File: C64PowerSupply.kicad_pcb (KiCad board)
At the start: 2 copper layers, 127 x 61 mm, 17 parts, among them J1 120V IN, J2 OUT, U1 LM2596T-ADJ

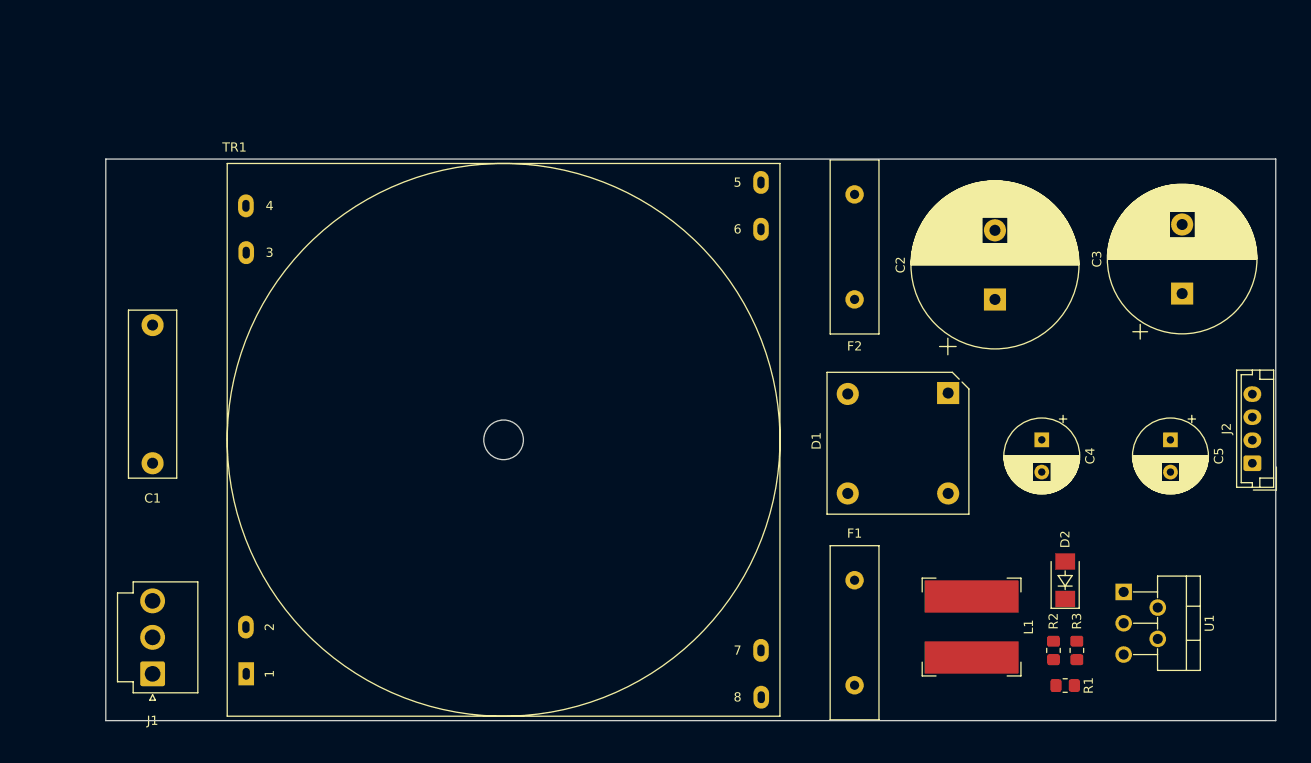
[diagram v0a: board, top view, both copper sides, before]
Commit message: Footprints, layout
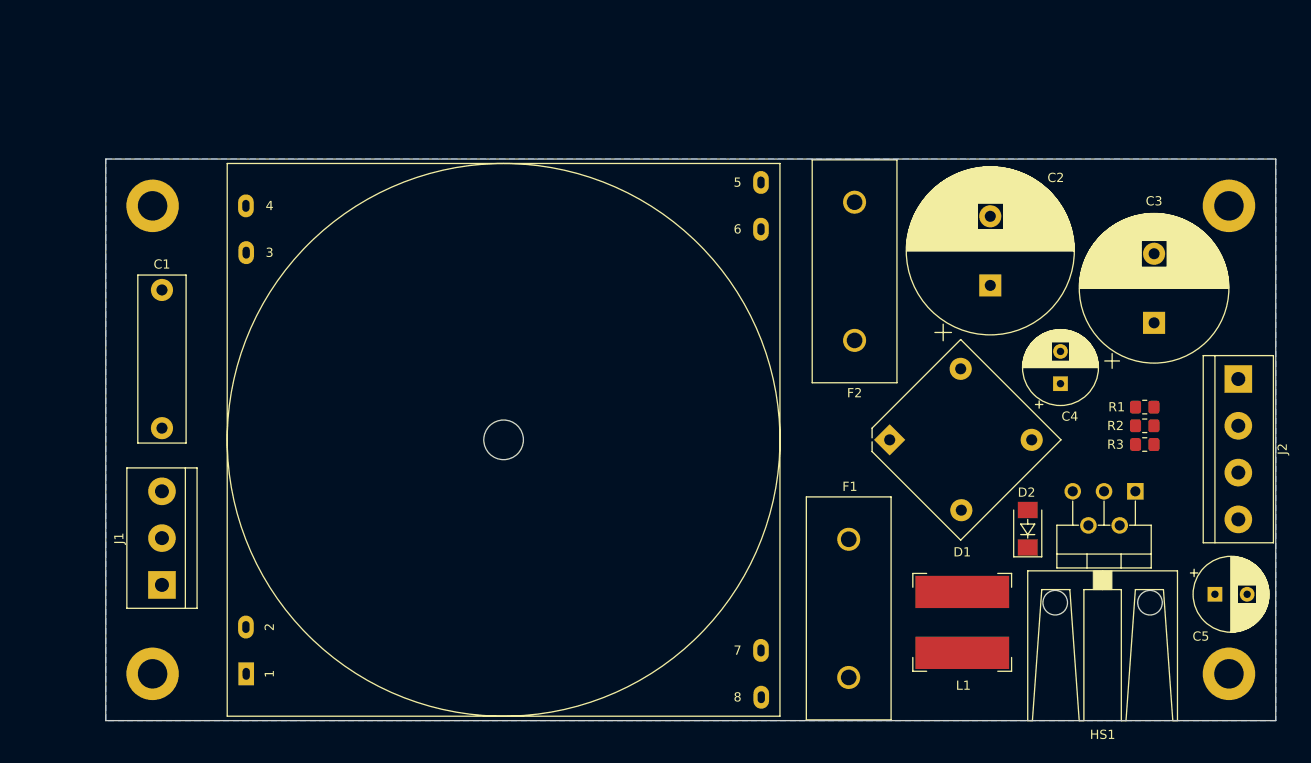
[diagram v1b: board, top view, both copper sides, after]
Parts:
- added H1: M3, MountingHole:MountingHole_3.2mm_M3_ISO7380_Pad, F.Cu at (73.7, 71.1)
- added H2: M3, MountingHole:MountingHole_3.2mm_M3_ISO7380_Pad, F.Cu at (190.5, 71.1)
- added H3: M3, MountingHole:MountingHole_3.2mm_M3_ISO7380_Pad, F.Cu at (190.5, 121.9)
- added H4: M3, MountingHole:MountingHole_3.2mm_M3_ISO7380_Pad, F.Cu at (73.7, 121.9)
- added HS1: Heatsink, DTLib:AAVID581002B02500G, F.Cu at (176.8, 110.7)
- F1, F2: footprint Fuse:Fuse_Littelfuse-LVR100 -> DTLib:Fuse_PTF-76
- J1: footprint Connector_JST:JST_VH_B3P-VH-B_1x03_P3.96mm_Vertical -> TerminalBlock:TerminalBlock_bornier-3_P5.08mm
- J2: footprint Connector_JST:JST_EH_B4B-EH-A_1x04_P2.50mm_Vertical -> TerminalBlock:TerminalBlock_bornier-4_P5.08mm
- moved R1 31.4 mm to (181.4, 93.0)
- moved R2 26.3 mm to (181.4, 95.0), turned to 180 degrees
- moved R3 23.5 mm to (181.4, 97.0), turned to 0 degrees
- moved C5 17.4 mm to (189.0, 113.3), turned to 0 degrees
- moved U1 11.0 mm to (180.3, 102.1), turned to 180 degrees
- moved J1 9.71 mm to (74.7, 112.3)
- moved J2 9.27 mm to (191.5, 89.9), turned to 270 degrees
- moved D1 8.13 mm to (153.7, 96.5), turned to 45 degrees
- moved D2 6.91 mm to (168.7, 106.2)
- moved C4 6.43 mm to (172.2, 90.4), turned to 90 degrees
- moved F1 4.49 mm to (149.2, 107.3)
- moved F2 4.44 mm to (149.9, 85.7)
- moved C3 4.40 mm to (182.4, 83.8)
- moved C1 3.94 mm to (74.7, 95.2)
- moved C2 1.61 mm to (164.6, 79.8)
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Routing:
- added copper zone on B.Cu, net GND

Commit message: Routing
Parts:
- R1, R2, R3: moved to B.Cu
- moved R1 20.3 mm to (176.8, 112.8)
- moved R2 16.4 mm to (176.8, 110.7), turned to 0 degrees
- moved F1 15.1 mm to (149.2, 122.4), turned to 90 degrees
- moved R3 12.5 mm to (176.8, 108.7), turned to 180 degrees
- moved C4 9.33 mm to (180.3, 95.0), turned to 180 degrees
- moved C5 1.02 mm to (188.0, 113.3)
- moved F2 0.51 mm to (149.4, 85.7)
- moved J2 0.51 mm to (191.0, 89.9)
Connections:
- net Net-(F1-Pad1) renamed /9VAC+
- net Net-(J2-Pad3) renamed /9VAC-
- J1 pad 1: /HOT -> GND
- J1 pad 3: GND -> /HOT
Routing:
- net GND: track 0.00 -> 308.1 mm
- net /9VAC-: track 0.00 -> 83.7 mm
- net /9VAC+: track 0.00 -> 67.8 mm
- net /VUNREG: track 0.00 -> 62.2 mm
- net VCC: track 0.00 -> 61.4 mm
- net /NEUTRAL: track 0.00 -> 57.0 mm
- net /HOT: track 0.00 -> 55.8 mm
- net Net-(D1-Pad2): track 0.00 -> 48.9 mm
- net Net-(F1-Pad2): track 0.00 -> 26.7 mm
- net /REG-OUT: track 0.00 -> 20.1 mm
- net Net-(D1-Pad4): track 0.00 -> 13.3 mm
- net Net-(F2-Pad2): track 0.00 -> 10.9 mm
- net /VADJ: track 0.00 -> 6.19 mm
- net Net-(R1-Pad2): track 0.00 -> 2.03 mm
- added copper zone on F.Cu, net GND
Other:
- net class MAINS added: clearance 0.5, trace_width 1, via_dia 1, via_drill 0.6
- board text added: "5VDC"
- board text added: "9VAC"
- board text added: "C64 Power Supply RevA 2021 Dominic Thibodeau https://github.com/hotkeysoft/c64PowerSupply-kicad dev@hotkeysoft.net"
- board text added: "GND"
- board text added: "H"
- board text added: "JLCJLCJLCJLC"
- board text added: "N"
- board text added: "WARNING 120 VAC"

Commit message: Added trimpot. Routing
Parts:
- removed R1: 4.7K, Resistor_SMD:R_0805_2012Metric_Pad1.20x1.40mm_HandSolder
- added RV1: 2K, Potentiometer_THT:Potentiometer_Bourns_3266W_Vertical, F.Cu at (179.3, 90.4)
- J1: footprint TerminalBlock:TerminalBlock_bornier-3_P5.08mm -> TerminalBlock_Phoenix:TerminalBlock_Phoenix_PT-1,5-3-5.0-H_1x03_P5.00mm_Horizontal
- J2: footprint TerminalBlock:TerminalBlock_bornier-4_P5.08mm -> TerminalBlock_Phoenix:TerminalBlock_Phoenix_PT-1,5-4-5.0-H_1x04_P5.00mm_Horizontal
- R2: value ADJ -> 1K8
- R3: value 1.5K -> 1K
- moved J2 14.7 mm to (191.0, 104.6), turned to 90 degrees
- moved R2 14.2 mm to (181.9, 97.5), turned to 270 degrees
- moved R3 13.2 mm to (183.9, 97.5), turned to 90 degrees
- moved J1 10.2 mm to (75.7, 102.1), turned to 270 degrees
- moved C4 8.62 mm to (174.2, 88.9)
- moved C3 0.72 mm to (181.9, 83.3)
- moved C2 0.51 mm to (164.1, 79.8)
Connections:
- J1 pad 1: GND -> /HOT
- J1 pad 3: /HOT -> GND
- J2 pad 1: GND -> /9VAC+
- J2 pad 2: VCC -> /9VAC-
- J2 pad 3: /9VAC- -> VCC
- J2 pad 4: /9VAC+ -> GND
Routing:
- net GND: track 308.1 -> 343.7 mm
- net /9VAC+: track 67.8 -> 82.0 mm
- net /VADJ: track 6.19 -> 16.7 mm
- net /VUNREG: track 62.2 -> 69.1 mm
- net VCC: track 61.4 -> 67.5 mm
- net Net-(R2-Pad1): track 2.03 -> 6.56 mm
- net Net-(F1-Pad2): track 26.7 -> 24.4 mm
- net Net-(D1-Pad2): track 48.9 -> 50.5 mm
- net /HOT: track 55.8 -> 56.5 mm
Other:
- net class MAINS: clearance 0.5 -> 1; trace_width 1 -> 1.2
- net class POWER added: clearance 0.5, trace_width 1.2, via_dia 1.2, via_drill 0.8
- board text added: "HOT"
- board text added: "NEUTRAL"
- board text added: "VADJUST"
- board text removed: "H"
- board text removed: "N"

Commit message: Kicad6 upgrade
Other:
- net class Default removed
- net class MAINS removed
- net class POWER removed

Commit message: wip
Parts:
- removed D2: SK33A-TP, DTLib:DO-214AC
- removed HS1: Heatsink, DTLib:AAVID581002B02500G
- added C6: 22μF, Capacitor_SMD:C_1210_3225Metric_Pad1.33x2.70mm_HandSolder, F.Cu at (177.5, 120.0)
- added R1: 1M, Resistor_THT:R_Axial_DIN0414_L11.9mm_D4.5mm_P15.24mm_Horizontal, F.Cu at (63.5, 114.3)
- added RV2: MOV, Varistor:RV_Disc_D9mm_W4mm_P5mm, F.Cu at (63.5, 82.5)
- added RV3: TVS, Diode_SMD:D_SMB_Handsoldering, F.Cu at (146.1, 95.2)
- added RV4: TVS, Diode_SMD:D_SMB_Handsoldering, F.Cu at (146.1, 76.2)
- added SW1: 120/240V SELECT, Button_Switch_THT:SW_E-Switch_EG1271_DPDT, F.Cu at (63.5, 88.9)
- C2: value 2200μF -> 0.1μF; footprint Capacitor_THT:CP_Radial_D18.0mm_P7.50mm -> Capacitor_SMD:C_0805_2012Metric_Pad1.18x1.45mm_HandSolder
- C5: value 220μF -> 22μF; footprint Capacitor_THT:CP_Radial_D8.0mm_P3.50mm -> Capacitor_SMD:C_1210_3225Metric_Pad1.33x2.70mm_HandSolder
- F2: value 1.5A -> 2.5A
- L1: value 33μH -> 10μH; footprint DTLib:L_Bourns-SRN1060 -> DTLib:L_BMRx00060630
- TR1: value 2x115V to 2x9V -> 2x115V to 2x8V; footprint DTLib:Transformer_L01_60x60 -> DTLib:Transformer_Hammond_183K16
- U1: value LM2596T-ADJ -> BD9E303EFJ-LBE2; footprint Package_TO_SOT_THT:TO-220-5_P3.4x3.7mm_StaggerOdd_Lead3.8mm_Vertical -> Package_SO:HTSOP-8-1EP_3.9x4.9mm_P1.27mm_EP2.4x3.2mm_ThermalVias
- moved C2 43.9 mm to (182.9, 119.4), turned to 0 degrees
- moved F2 41.6 mm to (190.4, 78.7), turned to 180 degrees
- moved C3 25.0 mm to (160.0, 71.1), turned to -90 degrees
- moved U1 12.3 mm to (172.7, 111.8), turned to 0 degrees
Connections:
- C1 pad 1: /HOT -> AC_HOT
- C1 pad 2: /NEUTRAL -> AC_NEUTRAL
- F1 pad 1: /9VAC+ -> /F_9VAC+
- F1 pad 2: Net-(F1-Pad2) -> /9VAC+
- F2 pad 1: Net-(D1-Pad4) -> /F_VCC
- F2 pad 2: Net-(F2-Pad2) -> VCC
- J1 pad 1: /HOT -> AC_HOT
- J1 pad 2: /NEUTRAL -> AC_NEUTRAL
- J2 pad 1: /9VAC+ -> /F_9VAC+
- J2 pad 3: VCC -> /F_VCC
- TR1 pad 1: /HOT -> AC_NEUTRAL
- TR1 pad 3: /HOT -> Net-(SW1-Pad5)
- TR1 pad 4: /NEUTRAL -> Net-(SW1-Pad2)
- TR1 pad 6: Net-(F2-Pad2) -> AC_HOT
- TR1 pad 7: /9VAC- -> /9VAC+
- U1 pad 1: /VUNREG -> unconnected-(U1-Pad1)
- U1 pad 2: /REG-OUT -> unconnected-(U1-Pad2)
- U1 pad 3: GND -> unconnected-(U1-Pad3)
- U1 pad 4: /VADJ -> unconnected-(U1-Pad4)
- U1 pad 5: GND -> (no net)
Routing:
- net GND: track 343.7 -> 0.00 mm
- net /9VAC-: track 84.1 -> 0.00 mm
- net /9VAC+: track 82.0 -> 0.00 mm
- net /VUNREG: track 69.1 -> 0.00 mm
- net VCC: track 67.5 -> 0.00 mm
- net /NEUTRAL: track 57.0 -> 0.00 mm
- net /HOT: track 56.5 -> 0.00 mm
- net Net-(D1-Pad2): track 50.5 -> 0.00 mm
- net Net-(F1-Pad2): track 24.4 -> 0.00 mm
- net /REG-OUT: track 20.1 -> 0.00 mm
- net /VADJ: track 16.7 -> 0.00 mm
- net Net-(D1-Pad4): track 13.3 -> 0.00 mm
- net Net-(F2-Pad2): track 10.9 -> 0.00 mm
- net Net-(R2-Pad1): track 6.56 -> 0.00 mm
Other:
- board text added: "C64 Power Supply RevB 2022 Dominic Thibodeau https://github.com/hotkeysoft/c64PowerSupply-kicad dev@hotkeysoft.net"
- board text removed: "C64 Power Supply RevA 2021 Dominic Thibodeau https://github.com/hotkeysoft/c64PowerSupply-kicad dev@hotkeysoft.net"
- board text removed: "JLCJLCJLCJLC"

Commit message: Begin route
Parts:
- removed the C4 at (174.2, 88.9)
- added C3: 10μF, Capacitor_SMD:C_1206_3216Metric_Pad1.33x1.80mm_HandSolder, F.Cu at (154.9, 105.4)
- added C5: 6800pF, Capacitor_SMD:C_0805_2012Metric_Pad1.18x1.45mm_HandSolder, F.Cu at (170.2, 113.0)
- added C6: 0.1μF, Capacitor_SMD:C_0805_2012Metric_Pad1.18x1.45mm_HandSolder, F.Cu at (167.6, 104.1)
- added J3: OUT C128, TerminalBlock_Phoenix:TerminalBlock_Phoenix_PT-1,5-4-5.0-H_1x04_P5.00mm_Horizontal, F.Cu at (188.0, 85.1)
- added JP1: GND LINK, Jumper:SolderJumper-2_P1.3mm_Bridged_Pad1.0x1.5mm, F.Cu at (76.2, 116.8)
- F2: value 2.5A -> 3A
- J2: value OUT -> OUT C64
- R1: value 1M -> 15K; footprint Resistor_THT:R_Axial_DIN0414_L11.9mm_D4.5mm_P15.24mm_Horizontal -> Resistor_SMD:R_0805_2012Metric_Pad1.20x1.40mm_HandSolder
- R2: value 1K8 -> 22K; moved to F.Cu
- R3: value 1K -> 5.6K; moved to F.Cu
- RV2: renamed from RV3; footprint Diode_SMD:D_SMB_Handsoldering -> Diode_SMD:D_SMB
- RV3: renamed from RV4; footprint Diode_SMD:D_SMB_Handsoldering -> Diode_SMD:D_SMB
- RV4: renamed from RV1; footprint Potentiometer_THT:Potentiometer_Bourns_3266W_Vertical -> Potentiometer_THT:Potentiometer_Bourns_3296W_Vertical
- SW1: footprint Button_Switch_THT:SW_E-Switch_EG1271_DPDT -> Button_Switch_THT:SW_NKK_G1xJP
- U1: footprint Package_SO:HTSOP-8-1EP_3.9x4.9mm_P1.27mm_EP2.4x3.2mm_ThermalVias -> Package_SO:Texas_HTSOP-8-1EP_3.9x4.9mm_P1.27mm_EP2.95x4.9mm_Mask2.4x3.1mm_ThermalVias
- moved R1 106.7 mm to (170.2, 118.1), turned to -90 degrees
- moved F1 79.4 mm to (104.0, 57.1), turned to 180 degrees
- moved F2 53.9 mm to (141.0, 57.1), turned to 0 degrees
- moved RV2 48.0 mm to (116.8, 57.1), turned to 0 degrees
- moved SW1 34.5 mm to (91.4, 109.2), turned to 180 degrees
- moved D1 31.2 mm to (164.7, 67.3), turned to 90 degrees
- moved C8 30.4 mm to (171.4, 90.2), turned to 180 degrees
- moved C4 29.9 mm to (154.7, 109.2), turned to 180 degrees
- moved RV3 26.1 mm to (128.3, 57.1), turned to 0 degrees
- moved C7 25.4 mm to (171.4, 94.0), turned to 180 degrees
- moved RV4 24.0 mm to (181.6, 114.3)
- moved R3 22.3 mm to (175.3, 118.1), turned to -90 degrees
- moved L1 20.1 mm to (176.5, 102.9), turned to 90 degrees
- moved RV1 20.0 mm to (78.7, 69.5), turned to 180 degrees
- moved R2 18.0 mm to (175.3, 114.3)
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- renumbered C3 to C2, C2 to C4, C5 to C7, C6 to C8, RV2 to RV1
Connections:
- net /9VAC+ renamed Net-(F1-Pad2)
- net /9VAC- renamed 9VAC_B
- net /F_9VAC+ renamed 9VAC_A
- C7 pad 1: VCC -> 5VDC
- C8 pad 1: VCC -> 5VDC
- F2 pad 1: /F_VCC -> Net-(D1-Pad4)
- F2 pad 2: VCC -> Net-(F2-Pad2)
- J1 pad 3: GND -> Earth
- J2 pad 3: /F_VCC -> 5VDC
- L1 pad 1: /REG-OUT -> /REG-SW
- L1 pad 2: VCC -> 5VDC
- R1 pad 1: AC_HOT -> Net-(C5-Pad1)
- R1 pad 2: AC_NEUTRAL -> GND
- R2 pad 2: /VADJ -> /FB
- R3 pad 1: /VADJ -> /FB
- RV3 pad 1: Net-(D1-Pad4) -> Net-(F2-Pad2)
- RV4 pad 1: VCC -> 5VDC
- TR1 pad 10: Net-(D1-Pad4) -> Net-(F2-Pad2)
- U1 pad 1: unconnected-(U1-Pad1) -> /BOOT
- U1 pad 2: unconnected-(U1-Pad2) -> /VUNREG
- U1 pad 3: unconnected-(U1-Pad3) -> /VUNREG
- U1 pad 4: unconnected-(U1-Pad4) -> GND
- U1 pad 5: (no net) -> /FB
- U1 pad 6: unconnected-(U1-Pad6) -> /COMP
- U1 pad 7: unconnected-(U1-Pad7) -> GND
- U1 pad 8: unconnected-(U1-Pad8) -> /REG-SW
- U1 pad 9: (no net) -> GND
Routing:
- net 9VAC_A: track 0.00 -> 141.8 mm
- net GND: track 0.00 -> 135.5 mm, vias 0 -> 56
- net 9VAC_B: track 0.00 -> 133.8 mm
- net AC_HOT: track 0.00 -> 133.0 mm
- net AC_NEUTRAL: track 0.00 -> 88.6 mm
- net 5VDC: track 0.00 -> 73.7 mm
- net Net-(D1-Pad2): track 0.00 -> 55.9 mm
- net /VUNREG: track 0.00 -> 53.1 mm
- net Net-(F2-Pad2): track 0.00 -> 45.6 mm
- net Net-(SW1-Pad5): track 0.00 -> 45.3 mm
- net Net-(F1-Pad2): track 0.00 -> 39.7 mm
- net Net-(SW1-Pad2): track 0.00 -> 39.0 mm
- net Net-(D1-Pad4): track 0.00 -> 27.2 mm
- net /REG-SW: track 0.00 -> 18.9 mm
- net Net-(SW1-Pad3): track 0.00 -> 17.8 mm
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- added copper zone on F.Cu, net /REG-SW
- added copper zone on F.Cu, net /VUNREG
- added copper zone on F.Cu, net 5VDC
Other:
- board size 127 x 61 mm -> 127 x 76.2 mm
- board text added: "120/240V SEL"
- board text added: "120V"
- board text added: "240V"
- board text added: "5VDC FUSE (2.5A)"
- board text added: "9VAC FUSE (1.5A)"
- board text added: "HOT SIDE"
- board text removed: "WARNING 120 VAC"

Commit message: Cleanup, fix 120/240V switch
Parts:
- added G***: LOGO, DTLib:Shock, F.Cu at (80.0, 120.7)
- added G***: LOGO, DTLib:Shock, B.Cu at (132.1, 111.8)
- F2: value 3A -> 2.5A
- SW1: footprint Button_Switch_THT:SW_NKK_G1xJP -> Button_Switch_THT:SW_NKK_GW12LJP
- moved SW1 5.08 mm to (91.4, 104.1), turned to -90 degrees
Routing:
- net Net-(SW1-Pad3): track 17.8 -> 2.54 mm
- net Net-(F1-Pad2): track 39.7 -> 46.6 mm
- net AC_HOT: track 133.0 -> 129.0 mm
- net Net-(SW1-Pad5): track 45.3 -> 41.3 mm
- net AC_NEUTRAL: track 88.6 -> 91.4 mm
- net 9VAC_B: track 133.8 -> 132.7 mm
- net 9VAC_A: track 141.8 -> 140.7 mm
- net Net-(F2-Pad2): track 45.6 -> 44.8 mm
- net /VUNREG: track 53.1 -> 52.6 mm
- net GND: vias 56 -> 62
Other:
- board text added: "C64/C128 Power Supply RevB 2022 Dominic Thibodeau https://github.com/hotkeysoft/c64PowerSupply-kicad dev@hotkeysoft.net"
- board text removed: "C64 Power Supply RevB 2022 Dominic Thibodeau https://github.com/hotkeysoft/c64PowerSupply-kicad dev@hotkeysoft.net"
